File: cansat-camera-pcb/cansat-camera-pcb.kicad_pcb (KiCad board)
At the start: 8 copper layers, 50 x 50 mm, 63 parts, among them IC2 TLV74315PDBVR, J1 Conn_01x08_Pin, J2 Micro_SD_Card_Det2, J4 Conn_02x10_Odd_Even, J5 Conn_02x10_Odd_Even, J6 OV5640, SW2 SW_Push, U1 IS42S16800F-5TLI, U2 AP2112K-3.3, U4 STM32H743ZITx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

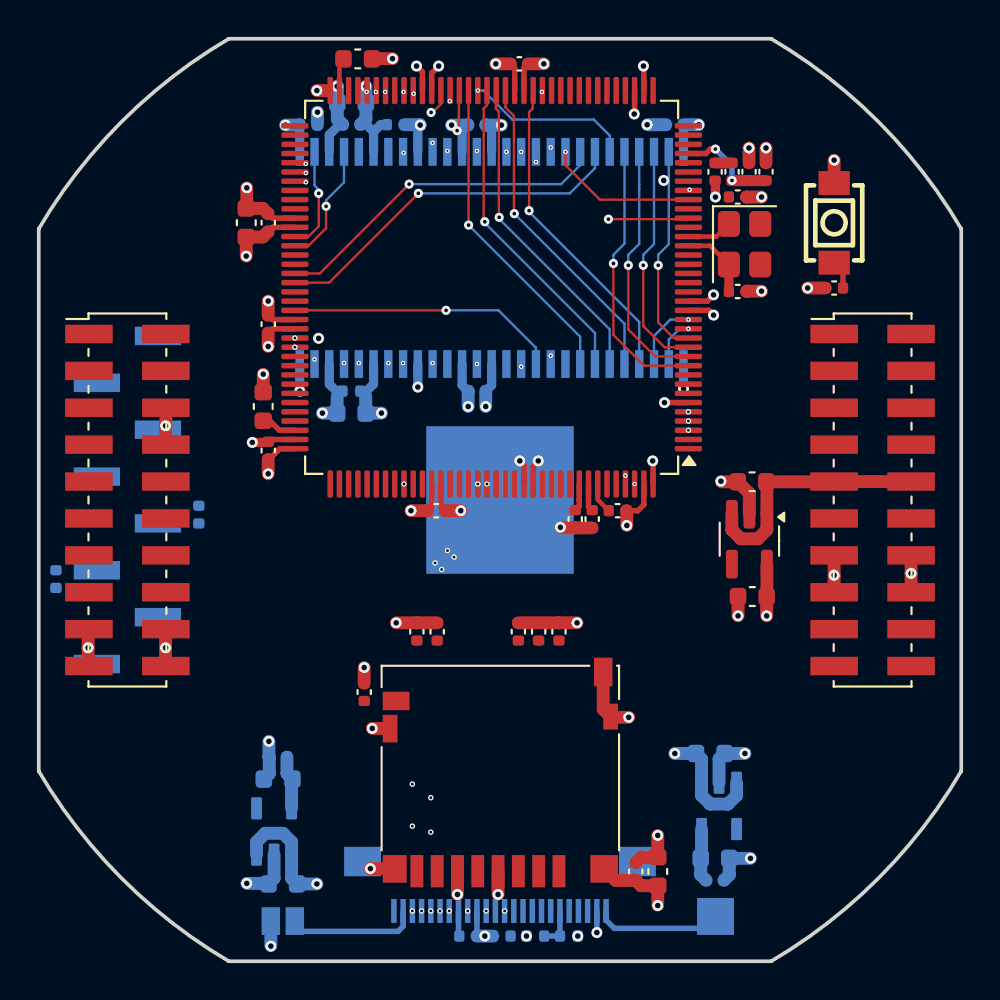
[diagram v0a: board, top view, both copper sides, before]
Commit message: Routing+SDram csere
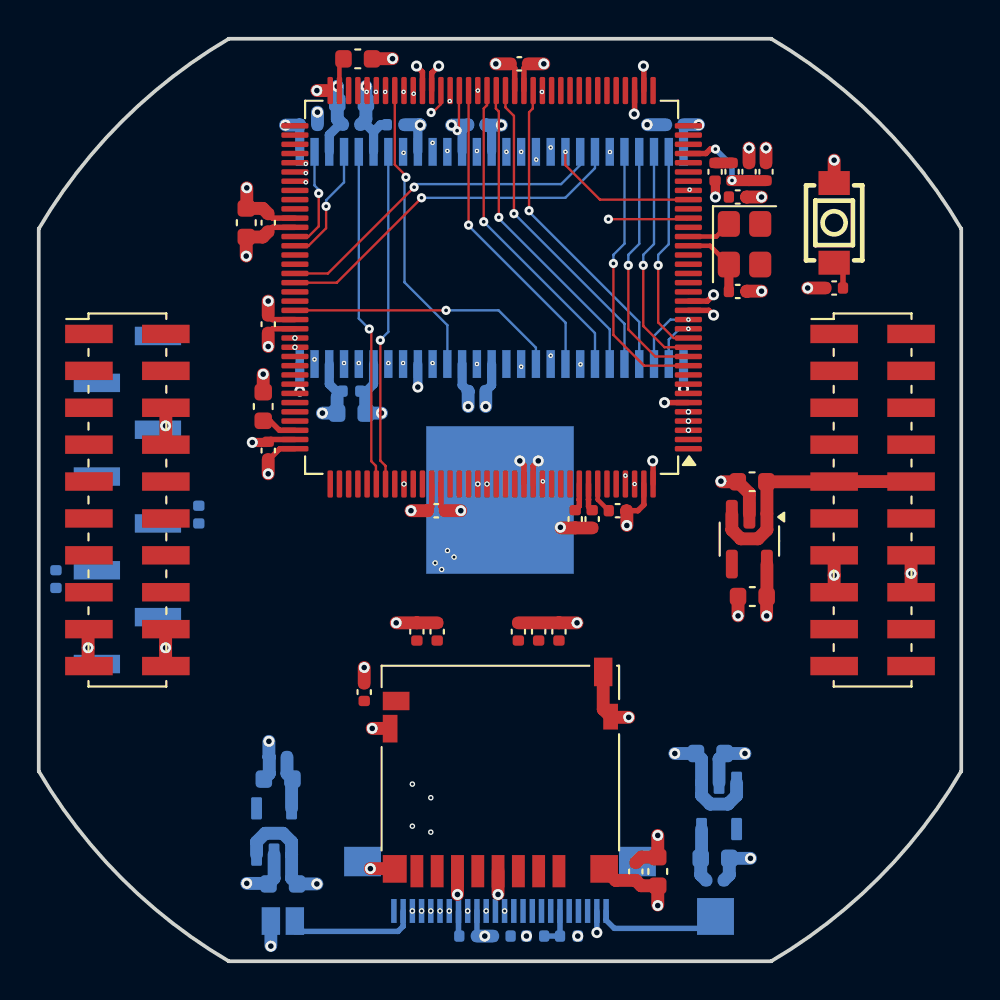
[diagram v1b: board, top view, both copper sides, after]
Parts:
- removed U1: IS42S16800F-5TLI, gaia-camera-footprints:IS42S16800F-5TLI
- added U3: W9825G6KH-6, Package_SO:TSOP-II-54_22.2x10.16mm_P0.8mm, B.Cu at (73.5, 114.5)
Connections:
- J2 pad 9: /sdcard/INSERTED -> /SDCARD_INSERTED
- R11 pad 2: /sdcard/INSERTED -> /SDCARD_INSERTED
- U4 pad 114: unconnected-(U4-PD0-Pad114) -> /FMC_D2
- U4 pad 115: unconnected-(U4-PD1-Pad115) -> /FMC_D3
- U4 pad 18: unconnected-(U4-PF6-Pad18) -> /FMC_AP
- U4 pad 7: unconnected-(U4-PC13-Pad7) -> /SDCARD_INSERTED
- U4 pad 89: /FMC_BA0 -> /FMC_BS0
- U4 pad 90: /FMC_BA1 -> /FMC_BS1
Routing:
- net /FMC_BS1: track 0.00 -> 19.7 mm, vias 0 -> 1
- net /FMC_BA1: track 19.7 -> 0.00 mm, vias 1 -> 0
- net /FMC_BS0: track 0.00 -> 18.6 mm, vias 0 -> 1
- net /FMC_BA0: track 18.6 -> 0.00 mm, vias 1 -> 0
- net /FMC_D2: track 0.00 -> 18.4 mm, vias 0 -> 1
- net /FMC_D3: track 0.00 -> 18.3 mm, vias 0 -> 1
- net /FMC_D9: track 0.00 -> 16.1 mm, vias 0 -> 1
- net /FMC_AP: track 0.00 -> 9.68 mm, vias 0 -> 2
- net /FMC_A10: track 9.04 -> 17.1 mm, vias 1 -> 2
- net GND: track 88.9 -> 88.1 mm
- net +3.3V: track 71.9 -> 71.7 mm, vias 33 -> 31

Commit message: Routolás SDkártya
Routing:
- net /SDMMC1_DAT0: track 0.00 -> 32.3 mm, vias 0 -> 3
- net /SDMMC1_DAT1: track 0.00 -> 31.9 mm, vias 0 -> 3
- net /SDMMC1_DAT2: track 0.00 -> 30.3 mm, vias 0 -> 3
- net /SDMMC1_DAT3: track 0.00 -> 28.5 mm, vias 0 -> 3
- net /SDMMC1_CMD: track 0.00 -> 24.5 mm, vias 0 -> 3
- net /SDMMC1_CK: track 0.00 -> 23.4 mm, vias 0 -> 2
- net /FMC_D15: track 11.2 -> 9.81 mm

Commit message: ready
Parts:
- removed J1: Conn_01x08_Pin, Connector_PinHeader_2.54mm:PinHeader_1x08_P2.54mm_Vertical_SMD_Pin1Left
- removed R4, R5: 10k, Capacitor_SMD:C_0402_1005Metric
- added C18: 100nF, Capacitor_SMD:C_0402_1005Metric, F.Cu at (81.5, 104.0)
- added C19: 100nF, Capacitor_SMD:C_0402_1005Metric, F.Cu at (70.0, 104.0)
- added C20: 100nF, Capacitor_SMD:C_0402_1005Metric, F.Cu at (83.6, 126.9)
- added C21: 100nF, Capacitor_SMD:C_0402_1005Metric, F.Cu at (85.6, 117.1)
- added C22: 100nF, Capacitor_SMD:C_0402_1005Metric, F.Cu at (75.5, 128.2)
- added C7: 100nF, Capacitor_SMD:C_0402_1005Metric, F.Cu at (63.3, 105.3)
- added J3: Conn_01x05_Socket, gaia-camera-footprints:PinSocket_1x05_P2.54mm_Horizontal, B.Cu at (59.4, 137.0)
- added R12: 10k, Resistor_SMD:R_0402_1005Metric, B.Cu at (61.8, 129.9)
- added R13: 10k, Resistor_SMD:R_0402_1005Metric, B.Cu at (61.8, 132.5)
- R1, R10, R11, R14, R15, R16, R17, R2, R3, R6, R7, R8, R9: footprint Capacitor_SMD:C_0402_1005Metric -> Resistor_SMD:R_0402_1005Metric
- moved C13 28.3 mm to (86.7, 122.3), turned to 180 degrees
- moved C8 25.3 mm to (86.6, 110.1)
- moved C6 7.10 mm to (61.5, 141.4), turned to 180 degrees
- moved C42 6.88 mm to (63.9, 148.1), turned to 90 degrees
- moved C11 5.50 mm to (61.4, 112.6)
- moved C44 4.30 mm to (61.7, 147.0), turned to 0 degrees
- moved C3 4.11 mm to (89.1, 107.7), turned to -90 degrees
- moved R1 2.92 mm to (86.3, 107.7), turned to 90 degrees
- moved R2 2.70 mm to (88.2, 107.7), turned to -90 degrees
- moved C36 2.39 mm to (60.1, 124.7), turned to 90 degrees
- moved C4 2.13 mm to (87.3, 107.7), turned to 90 degrees
- moved C43 1.88 mm to (84.0, 149.2), turned to -90 degrees
- moved IC2 1.41 mm to (61.9, 144.2), turned to -90 degrees
- moved C34 1.37 mm to (88.1, 110.9)
- moved C1 1.33 mm to (88.1, 116.3)
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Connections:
- J4 pad 1: /I2C2_SDA -> unconnected-(J4-Pin_1-Pad1)
- J4 pad 14: /USART2_TX -> /UART4_TX
- J4 pad 16: /USART2_RX -> /UART4_RX
- J4 pad 2: /I2C4_SDA -> unconnected-(J4-Pin_2-Pad2)
- J4 pad 3: /I2C2_SCL -> unconnected-(J4-Pin_3-Pad3)
- J4 pad 4: /I2C4_SCL -> unconnected-(J4-Pin_4-Pad4)
- U4 pad 103: unconnected-(U4-PA11-Pad103) -> /UART4_RX
- U4 pad 104: unconnected-(U4-PA12-Pad104) -> /UART4_TX
- U4 pad 69: /I2C2_SCL -> unconnected-(U4-PB10-Pad69)
- U4 pad 70: /I2C2_SDA -> unconnected-(U4-PB11-Pad70)
- U4 pad 75: /USART1_TX -> unconnected-(U4-PB14-Pad75)
- U4 pad 76: /USART1_RX -> unconnected-(U4-PB15-Pad76)
- U4 pad 81: /I2C4_SCL -> unconnected-(U4-PD12-Pad81)
- U4 pad 82: /I2C4_SDA -> unconnected-(U4-PD13-Pad82)
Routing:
- net /DCMI_PIXCLK: track 1.38 -> 54.9 mm, vias 0 -> 2
- net GND: track 88.1 -> 36.0 mm, vias 46 -> 176
- net /DCMI_HYSNC: track 0.00 -> 50.6 mm, vias 0 -> 2
- net /OV5640_PWDN: track 0.00 -> 42.9 mm, vias 0 -> 3
- net /OV5640_RESET: track 2.22 -> 41.9 mm, vias 0 -> 2
- net /OV5640_XCLK: track 0.00 -> 33.8 mm, vias 0 -> 3
- net /DCMI_VSYNC: track 0.00 -> 29.3 mm, vias 0 -> 2
- net /SDCARD_INSERTED: track 0.00 -> 29.1 mm, vias 0 -> 2
- net +3.3V: track 71.7 -> 43.7 mm, vias 31 -> 42
- net /I2C1_SDA: track 1.50 -> 28.2 mm, vias 0 -> 3
- net /I2C1_SCL: track 1.51 -> 26.3 mm, vias 0 -> 1
- net /BOOT0: track 1.69 -> 26.1 mm, vias 0 -> 1
- net /UART4_RX: track 0.00 -> 19.4 mm
- net /camera/1.5V_camera: track 2.91 -> 20.7 mm
- net /UART4_TX: track 0.00 -> 13.2 mm
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
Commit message: USB fix
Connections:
- J4 pad 12: unconnected-(J4-Pin_12-Pad12) -> /UART4_TX
- J4 pad 14: /UART4_TX -> /UART4_RX
- J4 pad 15: unconnected-(J4-Pin_15-Pad15) -> /usb_dm
- J4 pad 16: /UART4_RX -> /usb_dp
- U4 pad 75: unconnected-(U4-PB14-Pad75) -> /usb_dm
- U4 pad 76: unconnected-(U4-PB15-Pad76) -> /usb_dp
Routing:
- net /usb_dm: track 0.00 -> 31.2 mm
- net /usb_dp: track 0.00 -> 30.4 mm
- net /UART4_RX: track 19.4 -> 14.6 mm, vias 0 -> 2
- net /UART4_TX: track 13.2 -> 12.0 mm
- net /FMC_D13: track 16.7 -> 17.7 mm
- net GND: vias 176 -> 170

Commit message: Routolás sdram
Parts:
- removed U3: W9825G6KH-6, Package_SO:TSOP-II-54_22.2x10.16mm_P0.8mm
- added IC1: W9825G6JB-6I, Package_BGA:Alliance_TFBGA-54_8x8mm_Layout9x9_P0.8mm, B.Cu at (73.5, 116.1)
- moved C29 20.2 mm to (67.9, 120.2), turned to -90 degrees
- moved C32 16.5 mm to (71.5, 121.7), turned to 180 degrees
- moved C28 14.9 mm to (80.3, 119.0), turned to 90 degrees
- moved C30 13.5 mm to (79.1, 119.0), turned to 90 degrees
- moved C27 10.7 mm to (67.9, 116.9), turned to 90 degrees
- moved C33 7.94 mm to (66.7, 114.0), turned to 90 degrees
- moved C25 7.00 mm to (67.9, 114.0), turned to 90 degrees
- moved C26 6.91 mm to (74.4, 110.5), turned to 0 degrees
- moved C31 1.36 mm to (74.0, 121.7)
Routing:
- net /FMC_NBL0: track 21.2 -> 0.00 mm, vias 2 -> 0
- net /FMC_BS1: track 19.7 -> 0.00 mm, vias 1 -> 0
- net /FMC_BS0: track 18.6 -> 0.00 mm, vias 1 -> 0
- net /FMC_D2: track 18.4 -> 0.03 mm, vias 1 -> 0
- net /FMC_D3: track 18.2 -> 0.00 mm, vias 1 -> 0
- net /FMC_SDNCAS: track 17.8 -> 0.00 mm, vias 2 -> 0
- net /FMC_D13: track 17.7 -> 0.00 mm, vias 2 -> 0
- net /FMC_D8: track 17.1 -> 0.03 mm, vias 2 -> 0
- net /FMC_D9: track 16.1 -> 0.00 mm, vias 1 -> 0
- net /FMC_D10: track 15.9 -> 0.00 mm, vias 2 -> 0
- net /FMC_D11: track 15.6 -> 0.01 mm, vias 2 -> 0
- net /FMC_D14: track 15.2 -> 0.00 mm, vias 2 -> 0
- net /FMC_D15: track 15.1 -> 0.00 mm, vias 2 -> 0
- net /FMC_D12: track 15.8 -> 0.72 mm, vias 2 -> 0
- net GND: track 36.0 -> 21.5 mm, vias 170 -> 145
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
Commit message: Update cansat-camera-pcb.kicad_pcb
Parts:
- moved C32 10.1 mm to (79.1, 115.1), turned to 90 degrees
- moved C31 7.78 mm to (66.6, 119.3), turned to -90 degrees
- moved C29 0.48 mm to (67.8, 119.7)
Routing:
- net /DCMI_PIXCLK: track 54.9 -> 1.37 mm, vias 2 -> 0
- net +3.3V: track 29.7 -> 64.9 mm, vias 33 -> 43
- net /FMC_NBL1: track 0.00 -> 23.1 mm, vias 0 -> 3
- net /FMC_D7: track 0.00 -> 22.6 mm, vias 0 -> 3
- net /FMC_D5: track 0.00 -> 20.4 mm, vias 0 -> 3
- net /FMC_D4: track 0.03 -> 17.4 mm, vias 0 -> 3
- net /FMC_D6: track 0.00 -> 16.6 mm, vias 0 -> 3
- net /FMC_SDNRAS: track 0.00 -> 15.1 mm, vias 0 -> 3
- net /FMC_SDNCAS: track 0.00 -> 14.3 mm, vias 0 -> 2
- net /FMC_BS1: track 0.00 -> 14.1 mm, vias 0 -> 3
- net /FMC_SDNWE: track 0.08 -> 13.9 mm, vias 0 -> 3
- net /FMC_BS0: track 0.00 -> 13.3 mm, vias 0 -> 1
- net /FMC_SDNE0: track 0.00 -> 13.1 mm, vias 0 -> 3
- net /FMC_SDCKE0: track 0.00 -> 12.4 mm, vias 0 -> 1
- net /FMC_D1: track 0.00 -> 11.8 mm, vias 0 -> 2
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
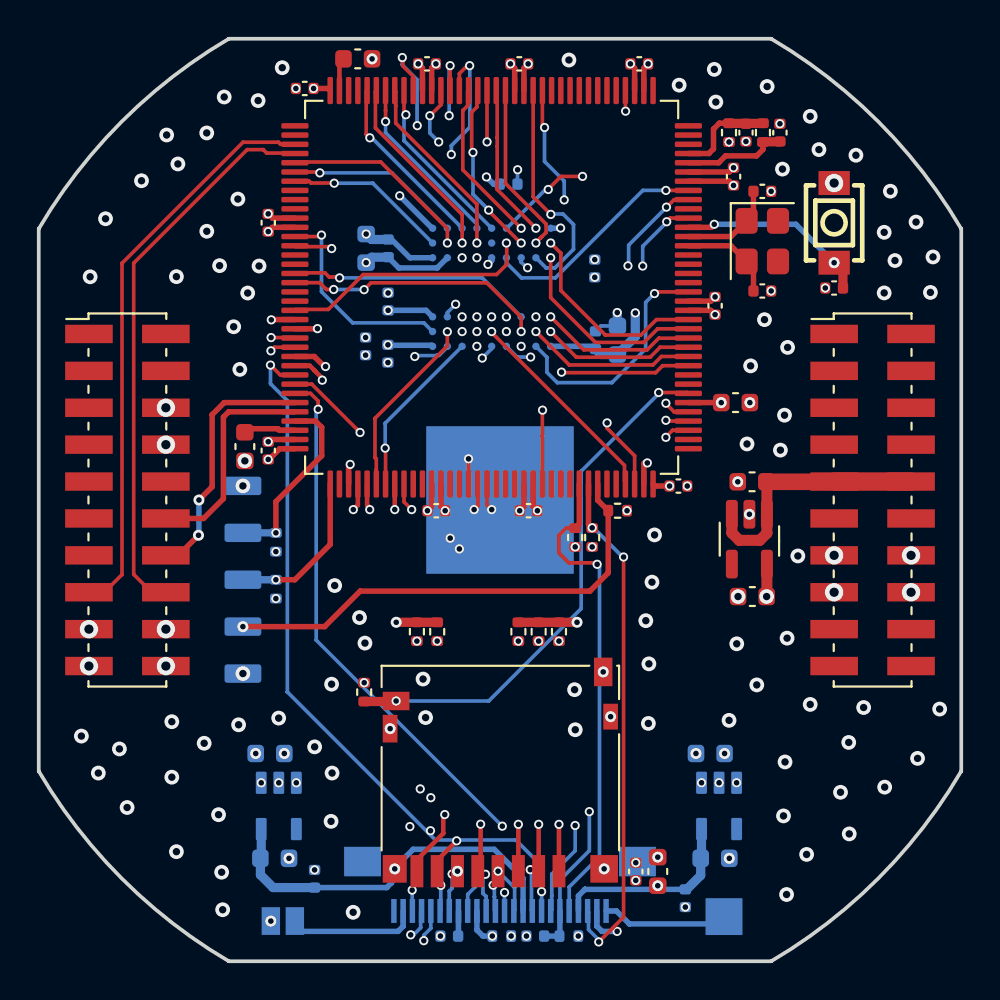
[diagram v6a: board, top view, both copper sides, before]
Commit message: sdcard deleted form this PCB
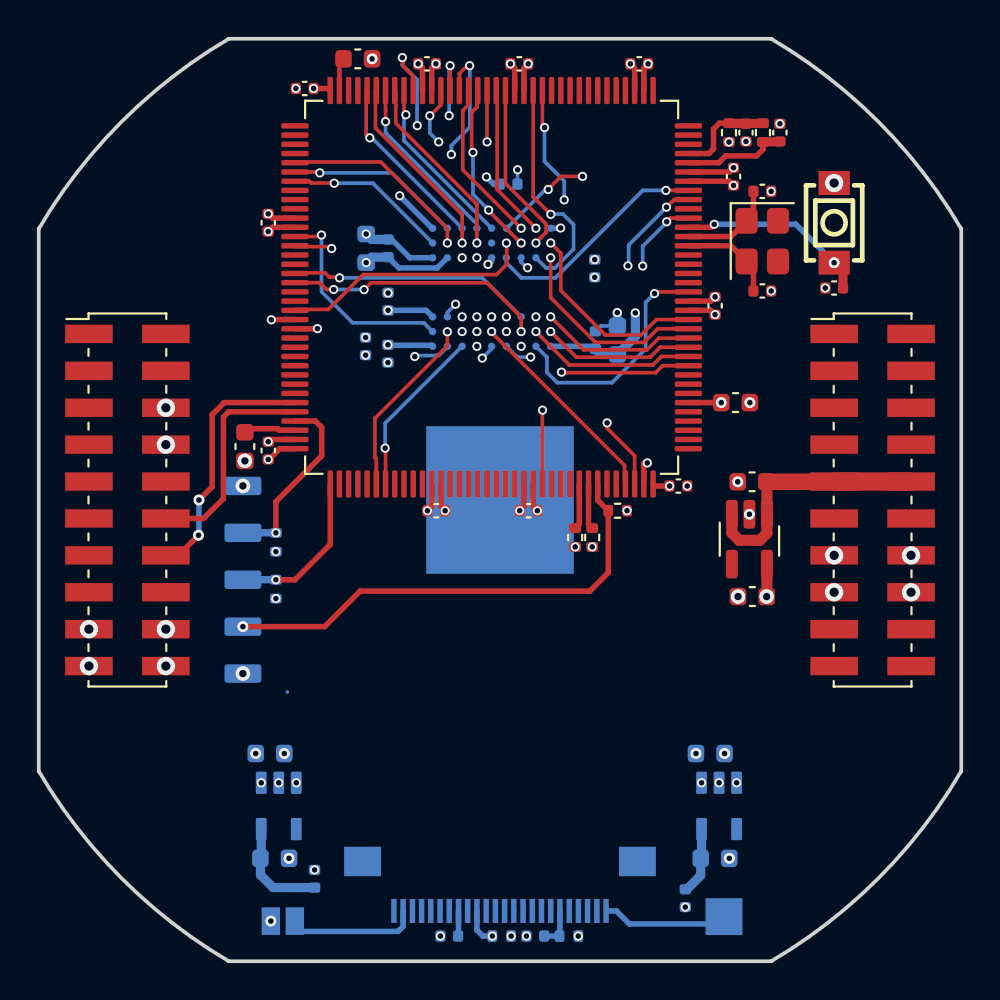
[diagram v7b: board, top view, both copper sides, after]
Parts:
- removed C16: 100nF, Capacitor_SMD:C_0402_1005Metric
- removed C17: 4.7uF, Capacitor_SMD:C_0603_1608Metric
- removed J2: Micro_SD_Card_Det2, Connector_Card:microSD_HC_Hirose_DM3D-SF
- removed R10, R6, R7, R8, R9: 10k, Resistor_SMD:R_0402_1005Metric
- removed R11: 47k, Resistor_SMD:R_0402_1005Metric
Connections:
- net /usb_dm renamed /usb_dn
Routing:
- net /DCMI_HYSNC: track 50.6 -> 0.07 mm, vias 2 -> 0
- net /OV5640_PWDN: track 42.9 -> 0.00 mm, vias 3 -> 1
- net /DCMI_D4: track 42.3 -> 0.00 mm, vias 2 -> 0
- net /DCMI_D6: track 40.8 -> 0.00 mm, vias 2 -> 0
- net /OV5640_RESET: track 41.7 -> 2.20 mm, vias 2 -> 0
- net /DCMI_D1: track 38.3 -> 0.00 mm, vias 2 -> 0
- net /DCMI_D7: track 37.8 -> 0.01 mm, vias 2 -> 0
- net /DCMI_D0: track 36.8 -> 0.06 mm, vias 2 -> 0
- net /OV5640_XCLK: track 33.8 -> 0.00 mm, vias 3 -> 0
- net /SDMMC1_DAT0: track 32.7 -> 0.00 mm, vias 3 -> 0
- net /SDMMC1_DAT1: track 32.1 -> 0.00 mm, vias 3 -> 0
- net /SDMMC1_DAT3: track 31.4 -> 0.00 mm, vias 3 -> 0
- net /usb_dn: track 31.2 -> 0.00 mm
- net /SDMMC1_DAT2: track 30.4 -> 0.00 mm, vias 3 -> 0
- net /usb_dp: track 30.4 -> 0.00 mm
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
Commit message: -
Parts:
- C40, C41, R16, R17: moved to F.Cu
- moved C41 2.22 mm to (77.7, 150.1), turned to 0 degrees
- moved R17 1.66 mm to (75.7, 151.1)
- moved C40 1.01 mm to (72.2, 151.1), turned to 0 degrees
- moved C20 0.64 mm to (83.1, 127.3), turned to 90 degrees
- moved R16 0.14 mm to (77.7, 151.1)
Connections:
- net /usb_dn renamed /usb_DN
- net /usb_dp renamed /usb_DP
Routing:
- net /DCMI_PIXCLK: track 1.37 -> 67.6 mm, vias 0 -> 3
- net /DCMI_HYSNC: track 0.07 -> 56.0 mm, vias 0 -> 2
- net /DCMI_D0: track 0.06 -> 41.7 mm, vias 0 -> 2
- net /DCMI_D6: track 0.00 -> 40.9 mm, vias 0 -> 2
- net /DCMI_D4: track 0.00 -> 40.2 mm, vias 0 -> 3
- net /DCMI_D7: track 0.01 -> 39.7 mm, vias 0 -> 2
- net /OV5640_PWDN: track 0.00 -> 39.4 mm, vias 1 -> 5
- net /OV5640_RESET: track 2.20 -> 39.3 mm, vias 0 -> 3
- net /DCMI_D1: track 0.00 -> 35.3 mm, vias 0 -> 2
- net /OV5640_XCLK: track 0.00 -> 34.6 mm, vias 0 -> 2
- net /usb_DN: track 0.00 -> 31.8 mm
- net /usb_DP: track 0.00 -> 31.8 mm
- net /DCMI_VSYNC: track 0.00 -> 25.5 mm, vias 0 -> 2
- net /DCMI_D5: track 0.00 -> 25.2 mm, vias 0 -> 2
- net /DCMI_D2: track 0.02 -> 25.0 mm, vias 0 -> 3
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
